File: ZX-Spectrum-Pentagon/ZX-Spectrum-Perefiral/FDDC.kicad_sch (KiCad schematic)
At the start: 0 parts

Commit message: update FDDC
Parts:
- added C? (x2): 20pF, Capacitor_SMD:C_0805_2012Metric_Pad1.18x1.45mm_HandSolder, symbol Device:C
- added R?: 2MOm, Resistor_SMD:R_0805_2012Metric_Pad1.20x1.40mm_HandSolder, symbol Device:R
- added U? (x2): 74HC74, symbol 74IEC:74HC74
- added U? (x2): 74HC04, Package_DIP:DIP-14_W7.62mm, symbol 74IEC:74HC04
- added U?: 74HC161, symbol 74IEC:74HC161
- added U? (x4): 74HC04, symbol 74IEC:74HC04
- added U?: 74HC283, symbol 74IEC:74HC283
- added Y?: 16MHz, Crystal:Crystal_HC49-U_Vertical, symbol Device:Crystal
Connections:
- new net: C?.1, R?.1, U?.1 (A), Y?.1
- new net: U?.10 (~{S}), U?.13 (~{R})
- new net: U?.12 (D), U?.8 (~{Q})
- new net: C?.1, R?.2, U?.2 (~{Y}), U?.3 (A), Y?.2
- new net: U?.2 (~{Y}), U?.6 (B0)
- new net: U?.2 (D), U?.6 (~{Q})
- new net: U?.11 (B3), U?.15 (B2), U?.4 (~{Y}), U?.7 (CI)
- new net 05MHz: U?.10 (S3), U?.11 (C), U?.11 (Q3), U?.12 (A3), U?.3 (A), U?.6 (D3)
- new net 1MHz: U?.1 (A), U?.12 (Q2), U?.13 (S2), U?.14 (A2), U?.5 (D2)
- new net 2MHz: U?.1 (S1), U?.13 (Q1), U?.3 (A1), U?.4 (D1)
- new net 4MHz: U?.14 (Q0), U?.3 (D0), U?.4 (S0), U?.5 (A0)
- new net GND: C?.2, C?.2, U?.7 (GND), U?.7 (GND), U?.7 (GND), U?.7 (GND), U?.7 (GND), U?.7 (GND), U?.7 (GND), U?.7 (GND), U?.8 (GND), U?.8 (GND)
- new net VCC: U?.07 (ECT), U?.1 (~{R}), U?.10 (ECR), U?.14 (VCC), U?.14 (VCC), U?.14 (VCC), U?.14 (VCC), U?.14 (VCC), U?.14 (VCC), U?.14 (VCC), U?.14 (VCC), U?.16 (VCC), U?.16 (VCC), U?.2 (B1)
- no-connect marks 0 -> 2

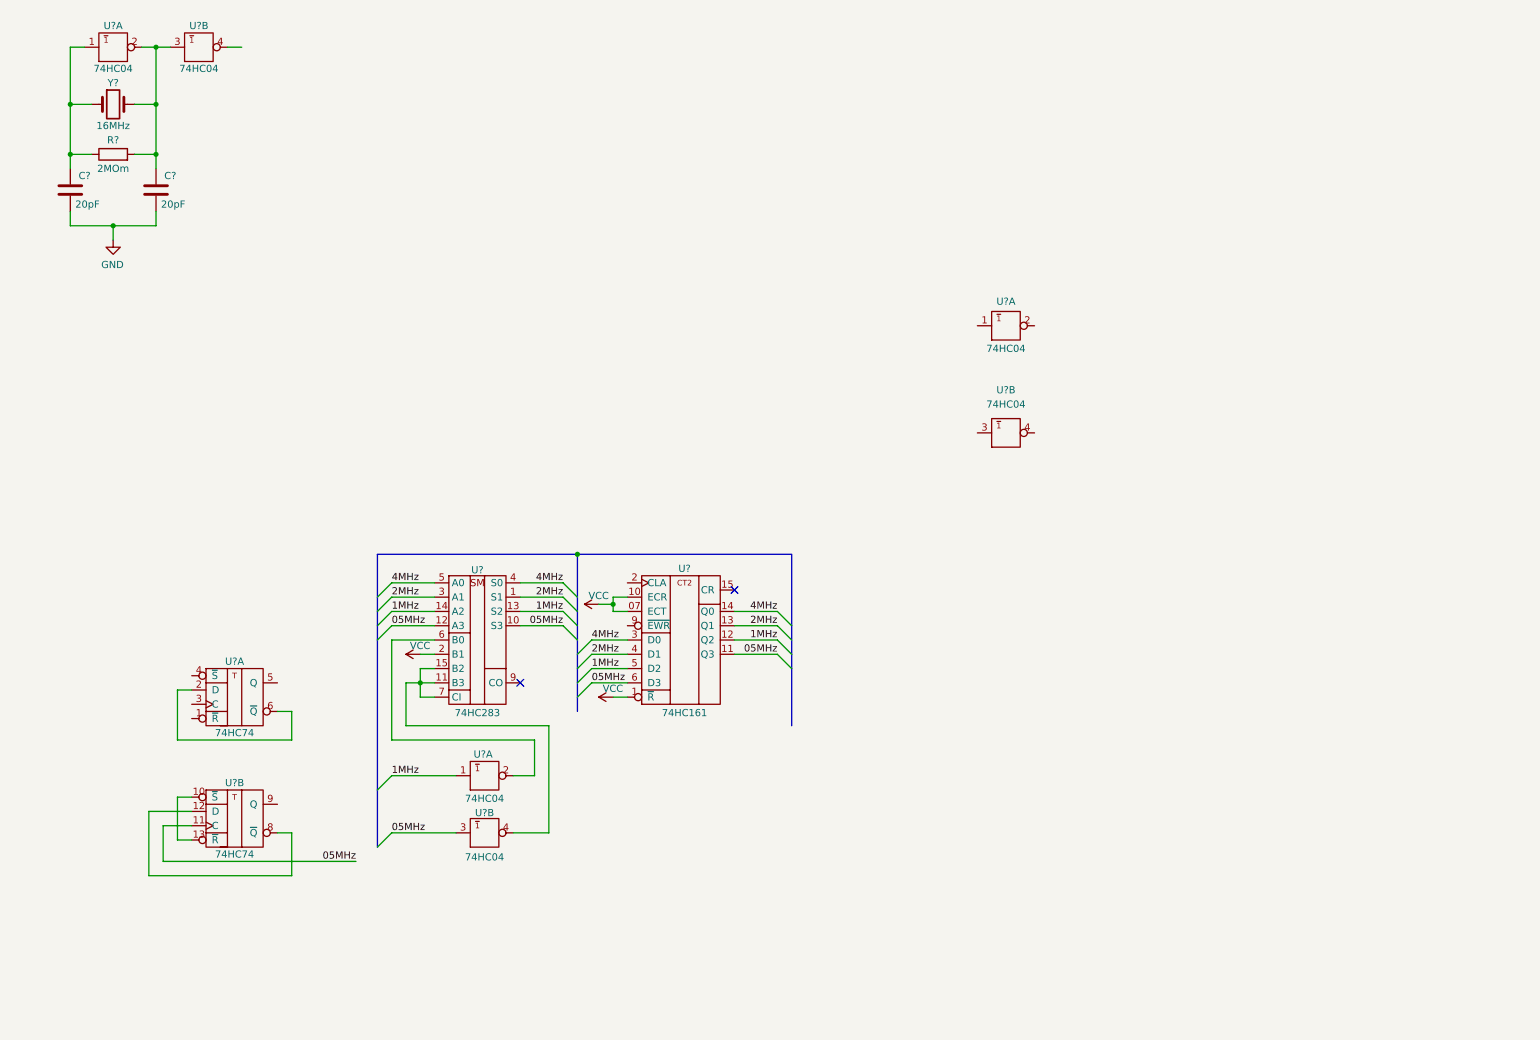
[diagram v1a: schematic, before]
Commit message: update schematic
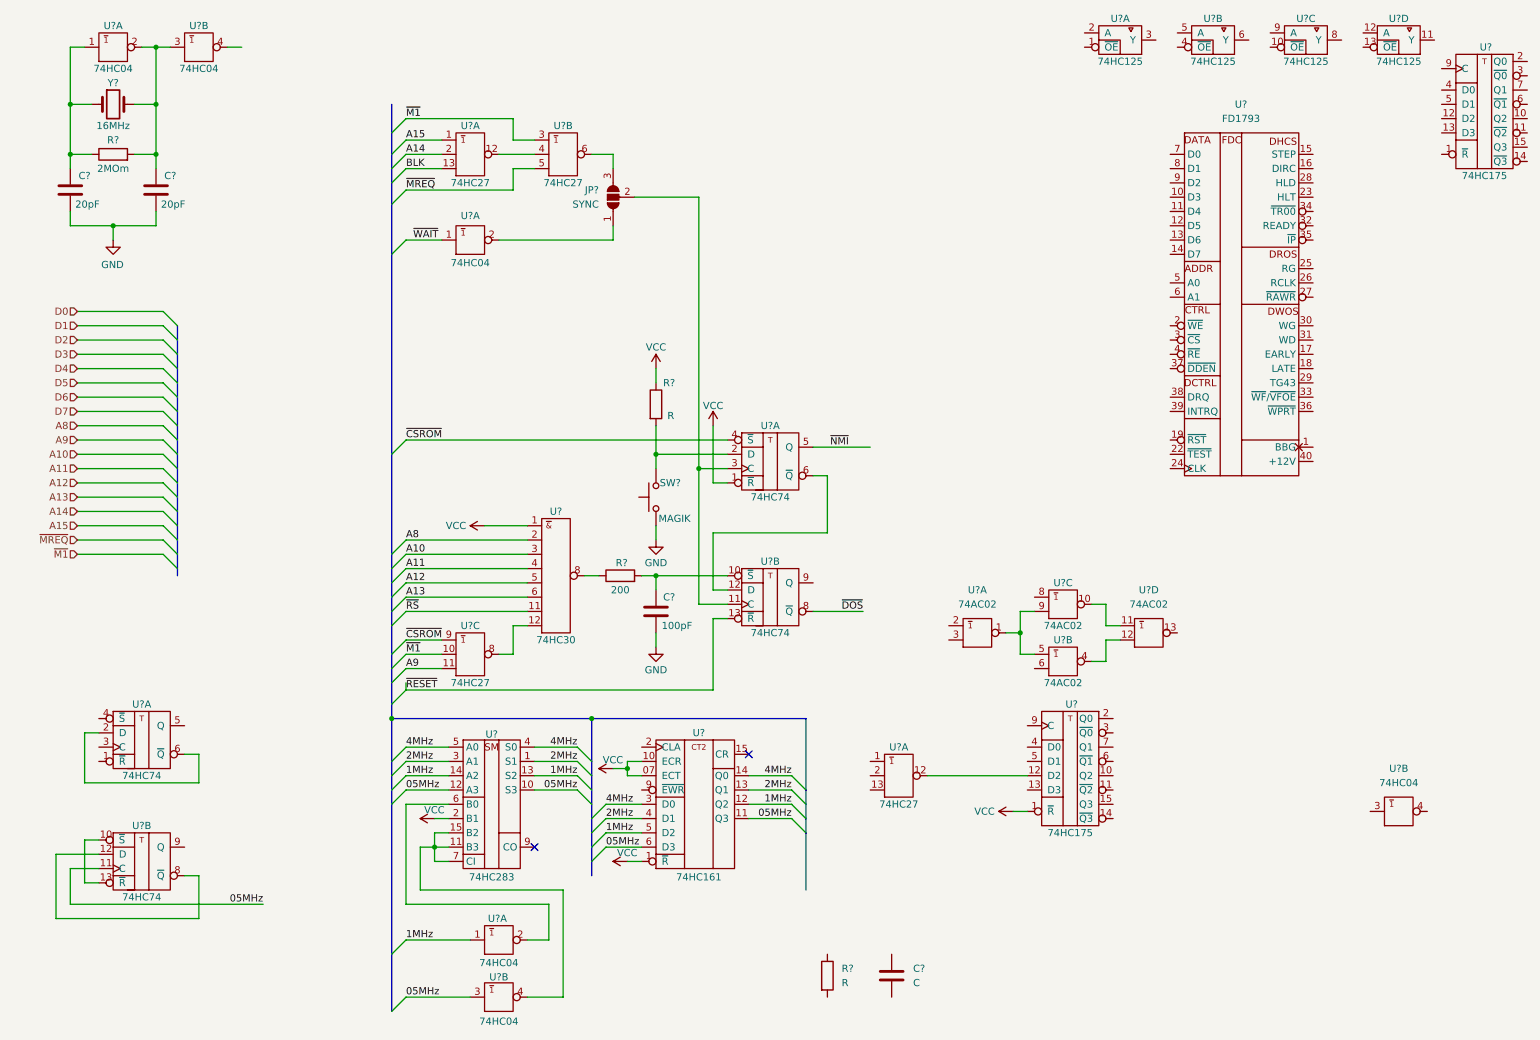
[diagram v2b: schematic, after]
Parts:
- added C?: C, Capacitor_SMD:C_0805_2012Metric, symbol Device:C
- added C?: 100pF, Capacitor_SMD:C_0805_2012Metric, symbol Device:C
- added JP?: SYNC, Jumper:SolderJumper-3_P1.3mm_Open_RoundedPad1.0x1.5mm, symbol Jumper:SolderJumper_3_Open
- added R?: 200, Resistor_SMD:R_0805_2012Metric, symbol Device:R
- added R? (x2): R, Resistor_SMD:R_0805_2012Metric, symbol Device:R
- added SW?: MAGIK, Button_Switch_THT:SW_Tactile_SPST_Angled_PTS645Vx31-2LFS, symbol Switch:SW_Push
- added U? (x4): 74HC27, symbol 74IEC:74HC27
- added U? (x2): 74HC175, symbol 74IEC:74HC175
- added U? (x4): 74AC02, symbol 74IEC:74AC02
- added U?: FD1793, Package_DIP:DIP-40_W15.24mm, symbol Controlers:FD1793
- added U? (x4): 74HC125, symbol 74IEC:74HC125
- added U? (x2): 74HC74, symbol 74IEC:74HC74
- added U?: 74HC30, symbol 74IEC:74HC30
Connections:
- net GND: now also C?.2, SW?.1, U?.10 (B), U?.10 (GND), U?.10 (GND), U?.10 (GND), U?.20 (GND), U?.7 (GND), U?.7 (GND), U?.7 (GND), U?.7 (GND), U?.7 (GND), U?.7 (GND), U?.7 (GND), U?.7 (GND), U?.7 (GND), U?.7 (GND), U?.7 (GND), U?.8 (GND), U?.8 (GND)
- net VCC: now also R?.1, U?.1 (A), U?.1 (~{R}), U?.1 (~{R}), U?.14 (VCC), U?.14 (VCC), U?.14 (VCC), U?.14 (VCC), U?.14 (VCC), U?.14 (VCC), U?.14 (VCC), U?.14 (VCC), U?.14 (VCC), U?.14 (VCC), U?.14 (VCC), U?.14 (VCC), U?.14 (VCC), U?.14 (VCC), U?.14 (VCC), U?.16 (VCC), U?.16 (VCC)
- net ~{WAIT}: now reaches U?.1 (A)
- net at U?.2 (~{Y}): now also JP?.1 (A)
- new net: U?.12 (~{Y}), U?.4 (B)
- new net: JP?.3 (B), U?.6 (~{Y})
- new net: U?.1 (~{Y}), U?.5 (A), U?.9 (B)
- new net: U?.12 (D2), U?.12 (~{Y})
- new net: JP?.2 (C), U?.11 (C), U?.3 (C)
- new net: U?.12 (B), U?.4 (~{Y})
- new net: R?.2, SW?.2, U?.2 (D)
- new net: U?.12 (D), U?.6 (~{Q})
- new net: U?.10 (~{Y}), U?.11 (A)
- new net: R?.1, U?.8 (~{Y})
- new net: C?.1, R?.2, U?.10 (~{S})
- new net: U?.12 (H), U?.8 (~{Y})
- new net A10: U?.3 (C)
- new net A11: U?.4 (D)
- new net A12: U?.5 (E)
- new net A13: U?.6 (F)
- new net A14: U?.2 (B)
- new net A15: U?.1 (A)
- new net A8: U?.2 (B)
- new net A9: U?.11 (C)
- new net BLK: U?.13 (C)
- new net VDD: U?.21 (VDD)
- new net ~{CSROM}: U?.4 (~{S}), U?.9 (A)
- new net ~{DOS}: U?.8 (~{Q})
- new net ~{M1}: U?.10 (B), U?.3 (A)
- new net ~{MREQ}: U?.5 (C)
- new net ~{NMI}: U?.5 (Q)
- new net ~{RESET}: U?.13 (~{R})
- new net ~{RS}: U?.11 (G)
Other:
- moved on the sheet: U?, U?A, U?B
